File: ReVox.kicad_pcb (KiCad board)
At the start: 2 copper layers, 60.8 x 86.2 mm, 42 parts, among them CN1 EXPANSION_PORT, CN2 AUDIO_OUT, CN3 AUDIO_OUT, U1 GAL20V8, U2 74LS273, U3 LM386

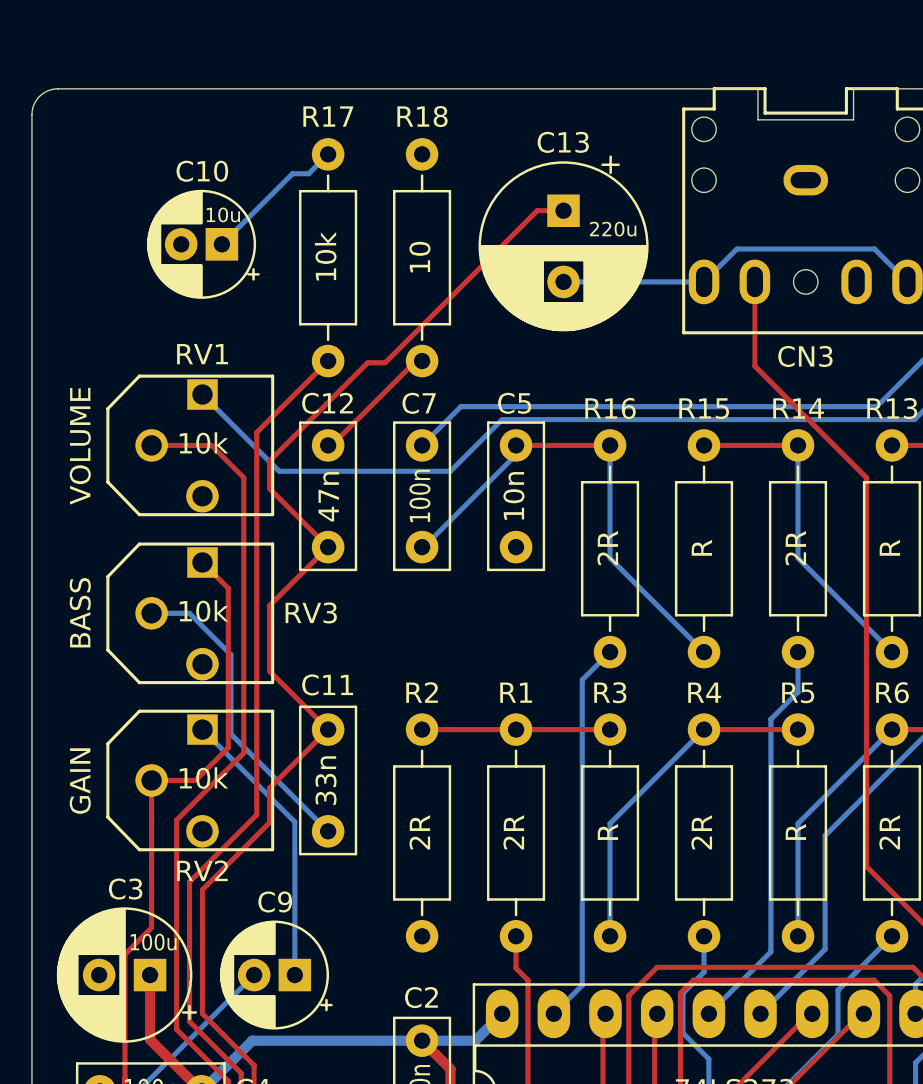
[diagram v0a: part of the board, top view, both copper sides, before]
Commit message: Add pin header with raw DAC signal, useful for testing
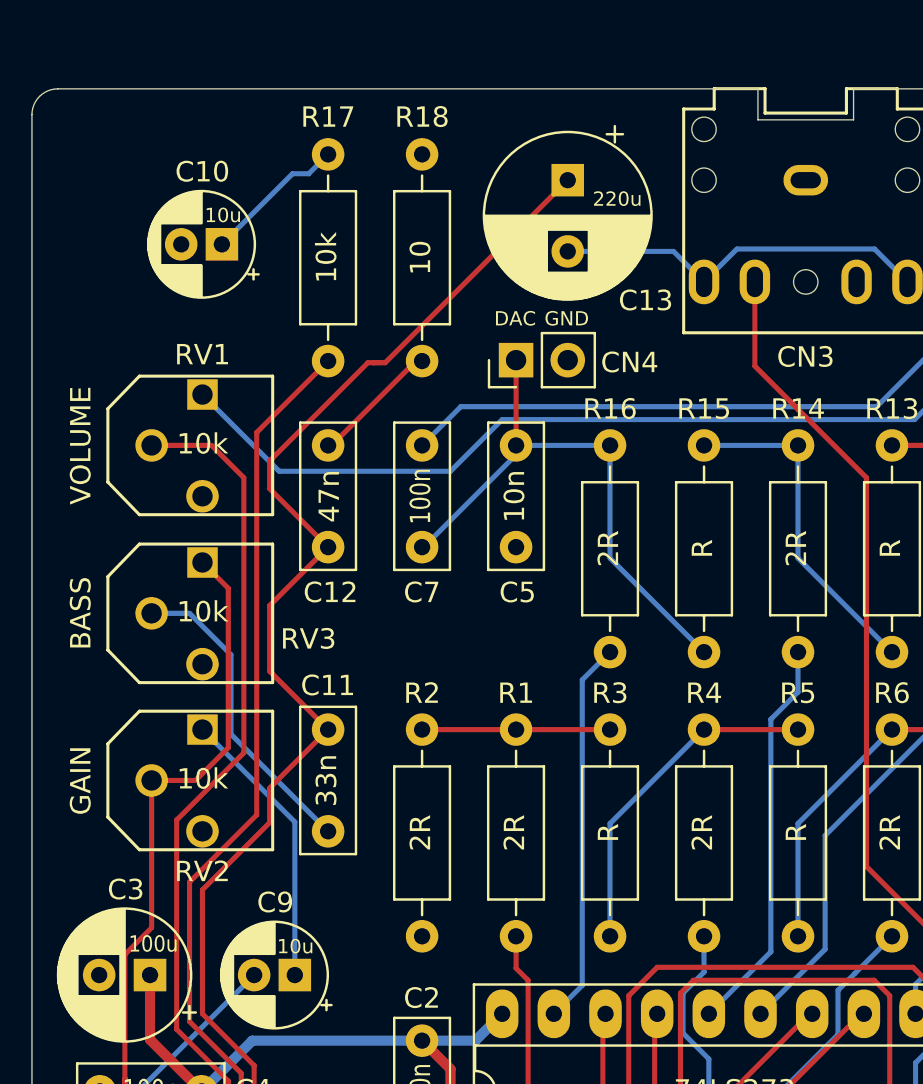
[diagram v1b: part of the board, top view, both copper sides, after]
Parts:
- added CN4: CN_RAW_DAC, Connector_PinHeader_2.54mm:PinHeader_1x02_P2.54mm_Vertical, F.Cu at (145.6, 75.2)
- moved C13 1.51 mm to (148.1, 66.3)
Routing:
- net Net-(C5-Pad2): track 23.7 -> 27.8 mm
- net Net-(C11-Pad1): track 61.5 -> 62.7 mm
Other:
- board text added: "DAC"
- board text added: "GND"

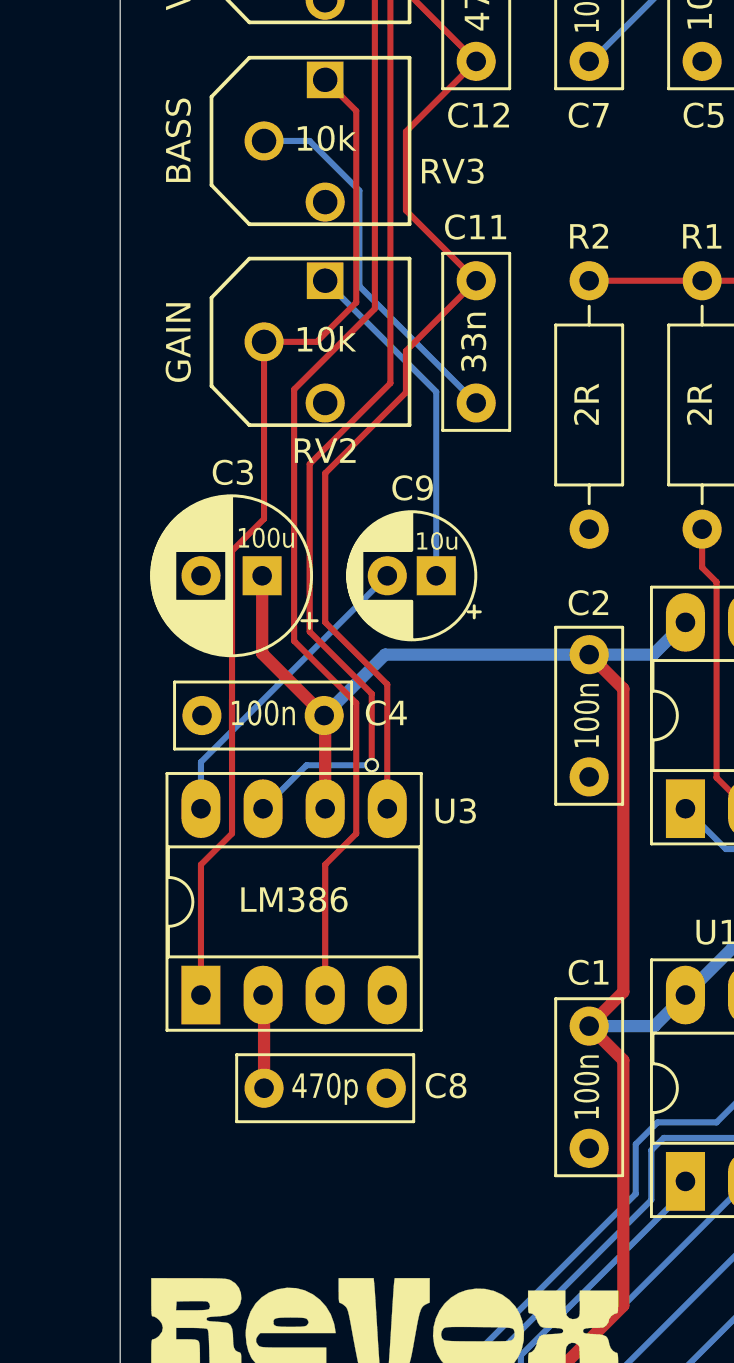
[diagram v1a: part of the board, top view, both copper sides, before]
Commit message: Improve RF immunity
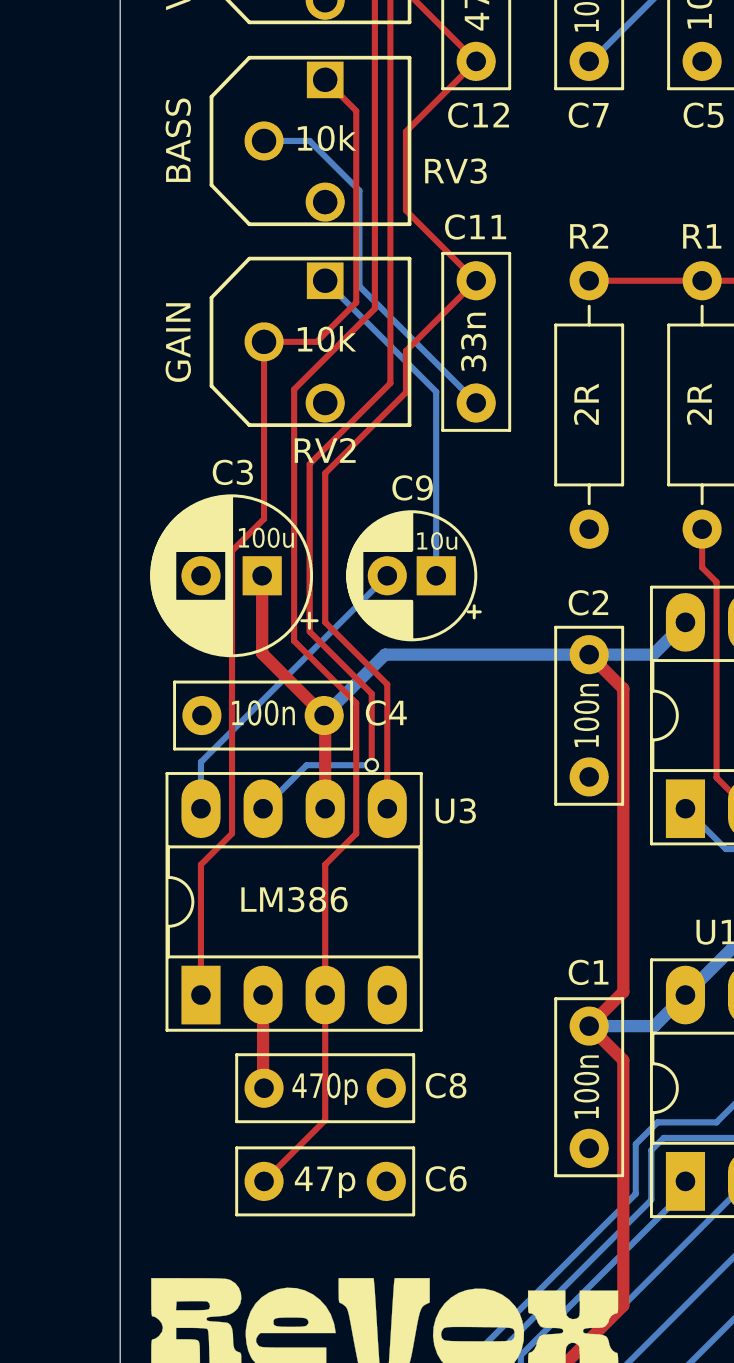
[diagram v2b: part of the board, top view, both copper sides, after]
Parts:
- added C6: 47p, Capacitor_THT:C_Disc_D7.0mm_W2.5mm_P5.00mm, F.Cu at (132.7, 130.2)
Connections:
- C8 pad 2: GND -> Net-(C8-Pad2)
- U3 pad 2: GND -> Net-(C8-Pad2)
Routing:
- net Net-(C6-Pad2): track 49.7 -> 58.4 mm
- net GND: track 24.7 -> 20.9 mm
- net Net-(C8-Pad2): track 0.00 -> 3.83 mm

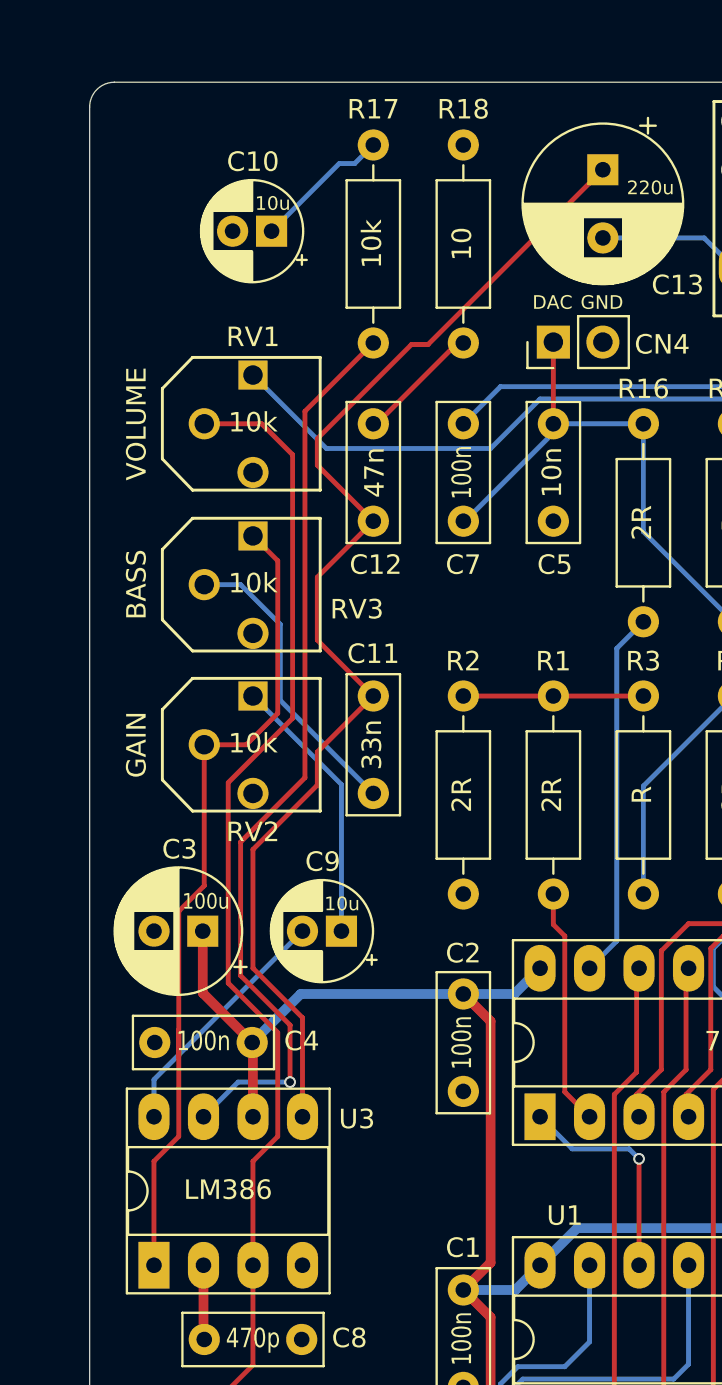
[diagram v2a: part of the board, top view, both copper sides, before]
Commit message: Add volume wiper series resistor
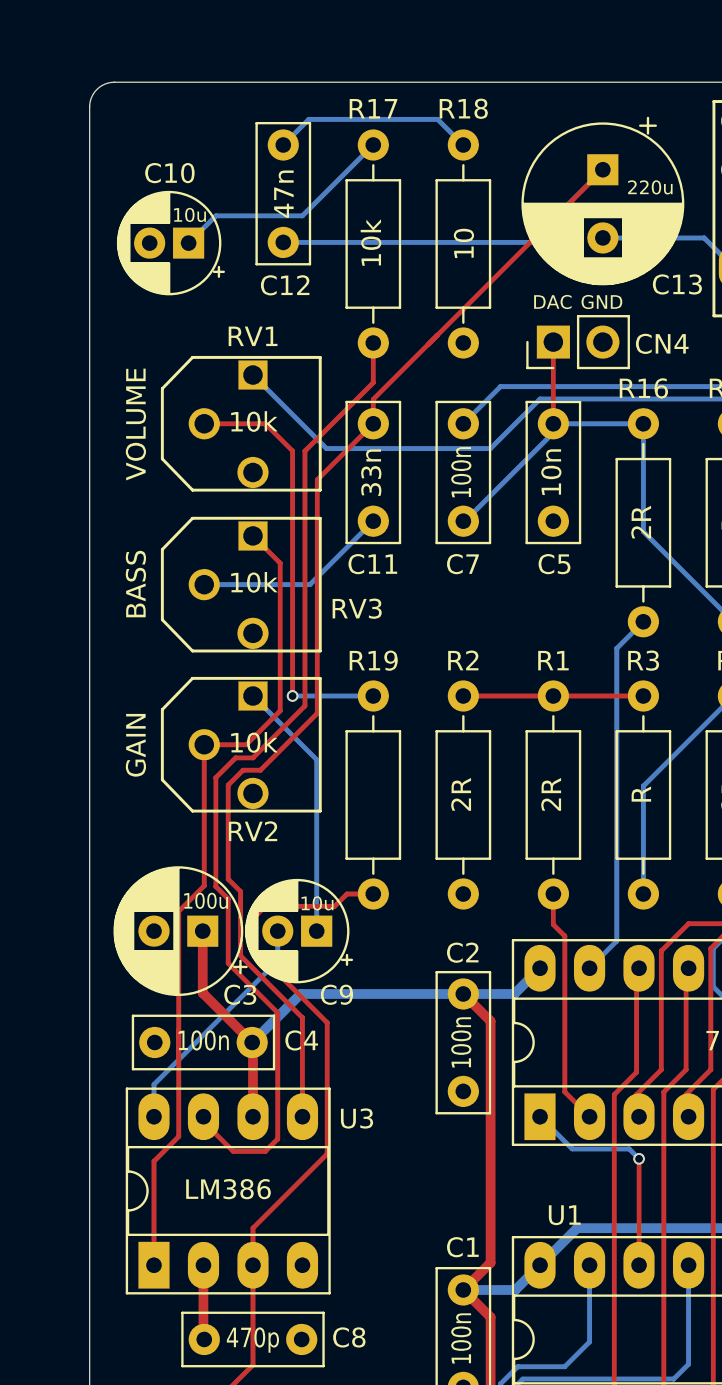
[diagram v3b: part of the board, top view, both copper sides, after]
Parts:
- added R19: 10k, Resistor_THT:R_Axial_DIN0207_L6.3mm_D2.5mm_P10.16mm_Horizontal, F.Cu at (136.4, 103.5)
- moved C12 15.0 mm to (131.7, 70.1)
- moved C11 14.0 mm to (136.4, 79.4)
- moved R18 10.2 mm to (141.0, 75.2), turned to 90 degrees
- moved C10 4.30 mm to (126.9, 70.1)
- moved C9 1.27 mm to (133.4, 105.4)
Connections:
- RV1 pad 2: Net-(C6-Pad2) -> Net-(R19-Pad2)
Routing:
- net Net-(C6-Pad2): track 58.4 -> 36.3 mm
- net Net-(R19-Pad2): track 0.00 -> 21.8 mm, vias 0 -> 1
- net Net-(C11-Pad1): track 62.7 -> 77.3 mm
- net Net-(C11-Pad2): track 15.4 -> 10.0 mm
- net Net-(C10-Pad1): track 7.05 -> 11.6 mm
- net Net-(R17-Pad2): track 47.0 -> 51.0 mm, vias 1 -> 0
- net Net-(C12-Pad2): track 6.34 -> 10.3 mm
- net Net-(C9-Pad2): track 12.7 -> 12.2 mm
- net Net-(C9-Pad1): track 13.9 -> 13.4 mm

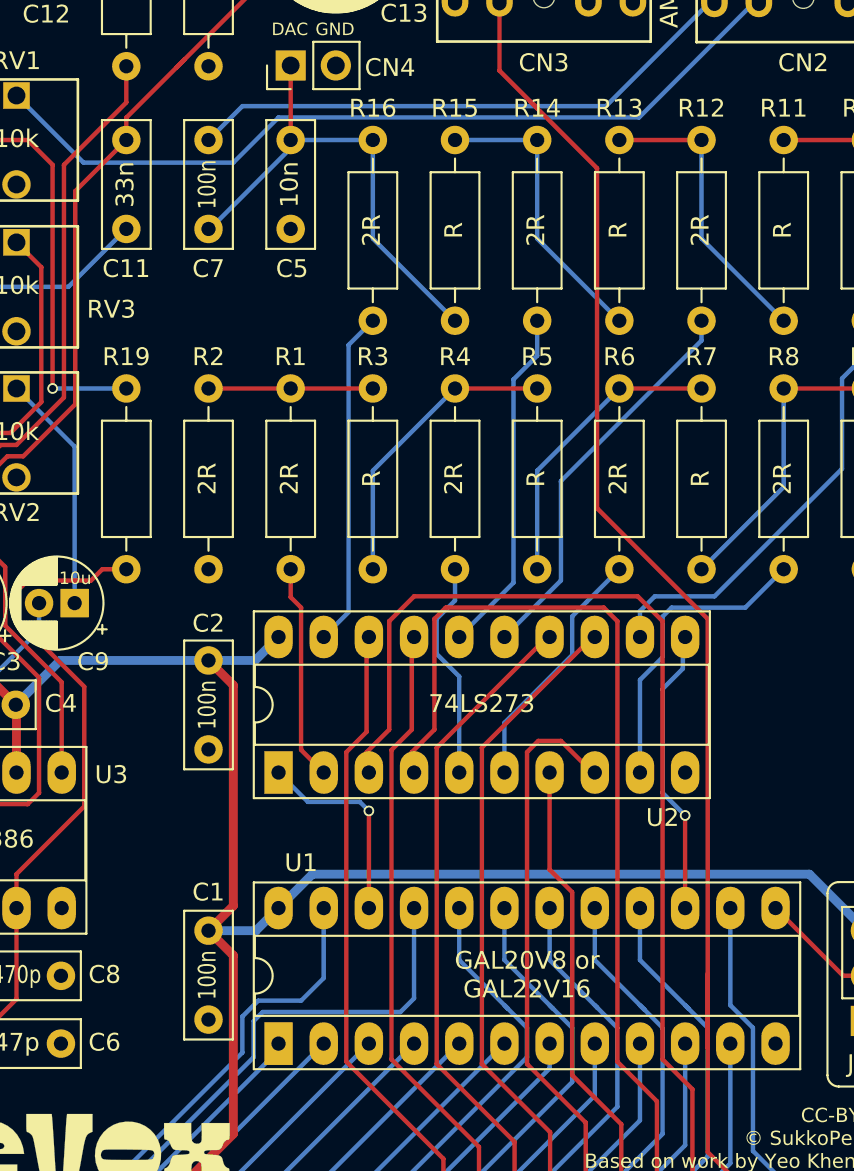
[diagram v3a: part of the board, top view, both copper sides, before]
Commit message: Some rerouting
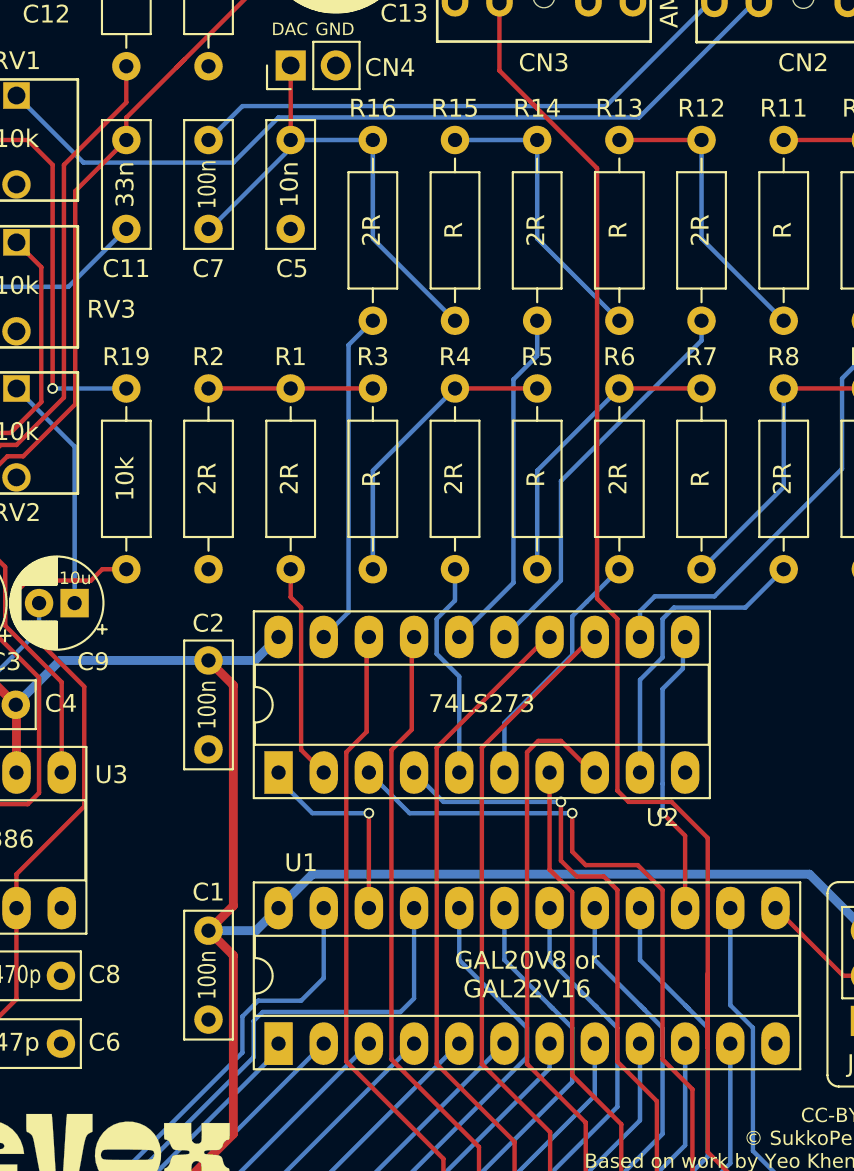
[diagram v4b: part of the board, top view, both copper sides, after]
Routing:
- net /d0: track 63.8 -> 43.7 mm, vias 0 -> 1
- net /d1: track 58.5 -> 39.5 mm, vias 0 -> 1
- net /ext_audio: track 83.6 -> 85.0 mm
